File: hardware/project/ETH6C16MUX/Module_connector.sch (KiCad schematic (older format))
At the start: 5 parts, among them J901 Conn_02x12_Odd_Even

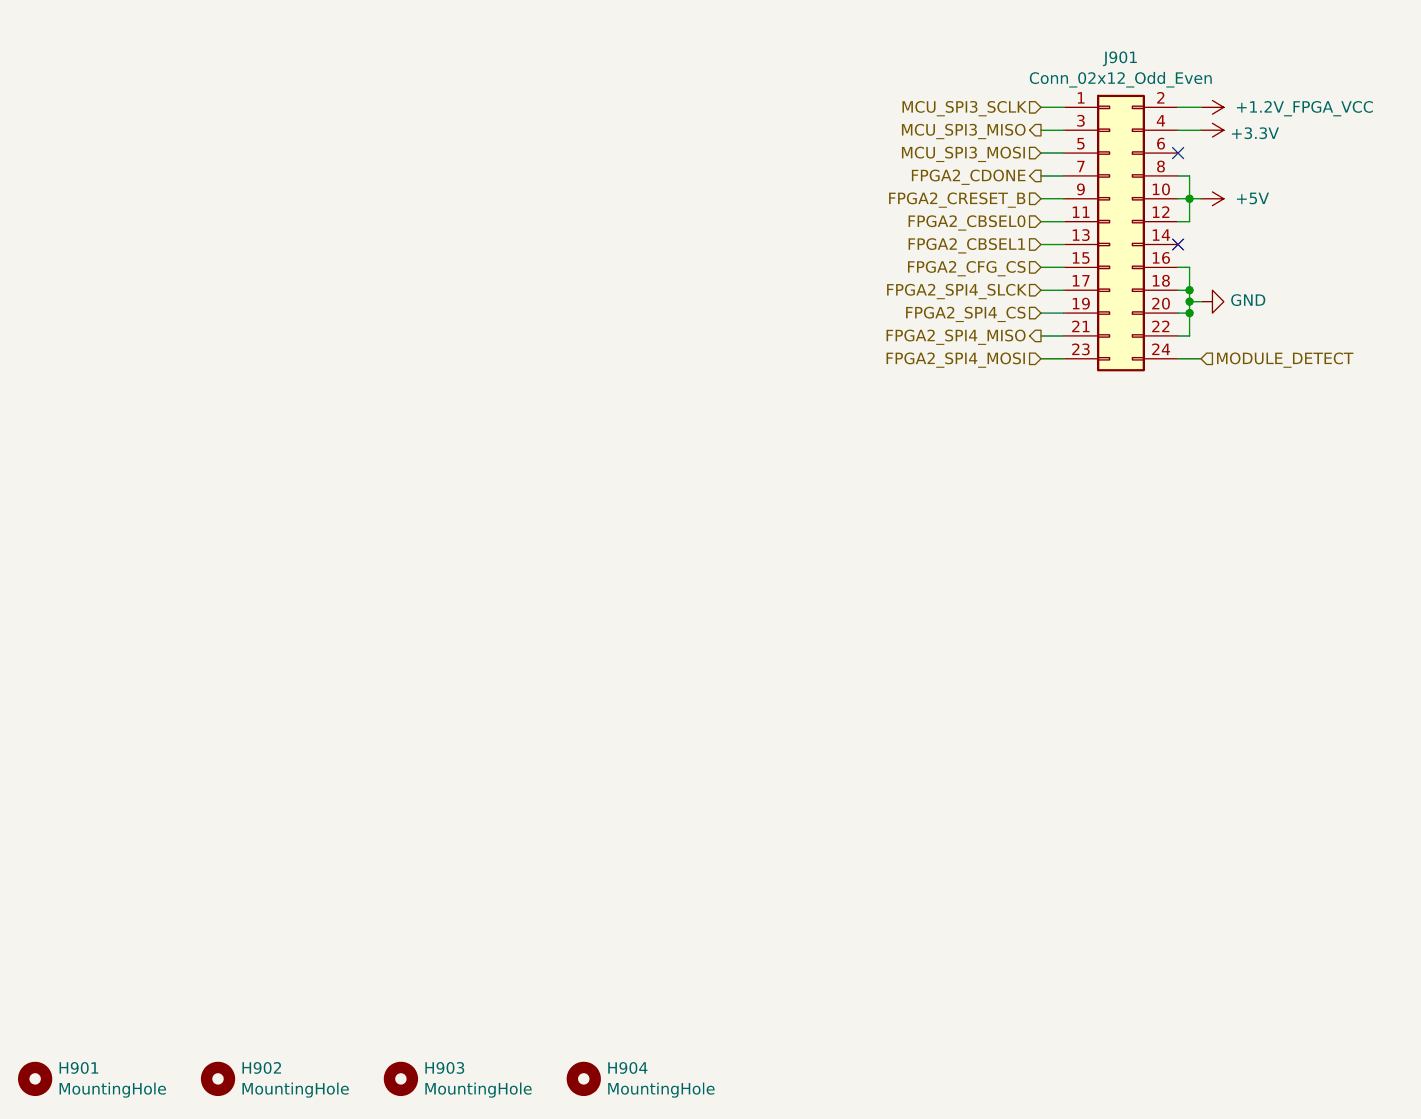
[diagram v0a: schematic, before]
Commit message: PCB design, need to redesign of the board to board connectors.
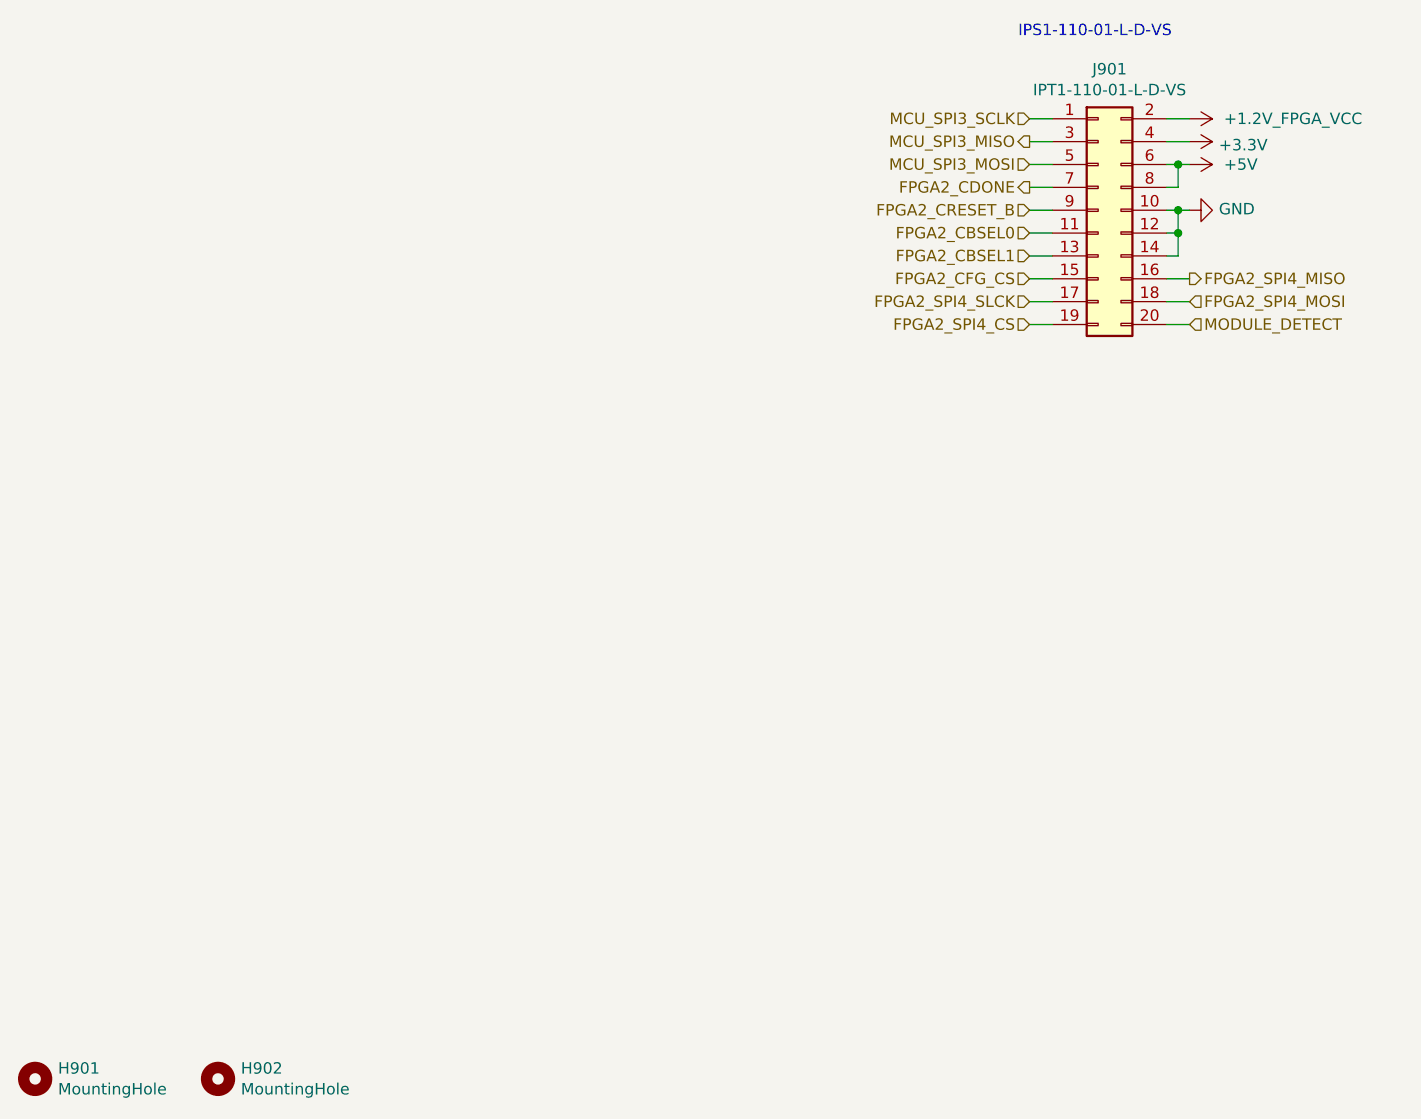
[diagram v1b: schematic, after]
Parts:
- removed H903, H904: MountingHole, symbol Mechanical:MountingHole
- removed J901: Conn_02x12_Odd_Even, symbol Connector_Generic:Conn_02x12_Odd_Even
- added J901: IPT1-110-01-L-D-VS, Connector_PinHeader_2.54mm:PinHeader_2x10_P2.54mm_Vertical_SMD, symbol Connector_Generic:Conn_02x10_Odd_Even
- H901, H902: footprint (none) -> MountingHole:MountingHole_3mm_Pad
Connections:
- net +1.2V_FPGA_VCC: now also J901.2 (Pin_2)
- net +3V3: now also J901.4 (Pin_4)
- net +5V: now also J901.6 (Pin_6), J901.8 (Pin_8)
- net FPGA2_CBSEL0: now also J901.11 (Pin_11)
- net FPGA2_CBSEL1: now also J901.13 (Pin_13)
- net FPGA2_CDONE: now also J901.7 (Pin_7)
- net FPGA2_CFG_CS: now also J901.15 (Pin_15)
- net FPGA2_CRESET_B: now also J901.9 (Pin_9)
- net FPGA2_SPI4_CS: now also J901.19 (Pin_19)
- net FPGA2_SPI4_MISO: now also J901.16 (Pin_16)
- net FPGA2_SPI4_MOSI: now also J901.18 (Pin_18)
- net FPGA2_SPI4_SLCK: now also J901.17 (Pin_17)
- net GND: now also J901.10 (Pin_10), J901.12 (Pin_12), J901.14 (Pin_14)
- net MCU_SPI3_MISO: now also J901.3 (Pin_3)
- net MCU_SPI3_MOSI: now also J901.5 (Pin_5)
- net MCU_SPI3_SCLK: now also J901.1 (Pin_1)
- net MODULE_DETECT: now also J901.20 (Pin_20)
- no-connect marks 2 -> 0
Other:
- note added: "IPS1-110-01-L-D-VS"
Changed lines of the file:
@@
 $EndDescr
-$Comp
-L Connector_Generic:Conn_02x12_Odd_Even J901
-U 1 1 5D9271DE
-P 5750 3250
-F 0 "J901" H 5800 3967 50  0000 C CNN
-F 1 "Conn_02x12_Odd_Even" H 5800 3876 50  0000 C CNN
-F 2 "" H 5750 3250 50  0001 C CNN
-F 3 "~" H 5750 3250 50  0001 C CNN
-	1    5750 3250
-	1    0    0    -1
-$EndComp
 $Comp
 L ETH6C16MUX:+1.2V_FPGA_VCC #PWR0901
 U 1 1 5D928C56
-P 6150 2750
-F 0 "#PWR0901" H 6150 2600 50  0001 C CNN
-F 1 "+1.2V_FPGA_VCC" V 6150 2900 50  0000 L CNN
-F 2 "" H 6150 2750 50  0001 C CNN
-F 3 "" H 6150 2750 50  0001 C CNN
-	1    6150 2750
+P 6100 2800
+F 0 "#PWR0901" H 6100 2650 50  0001 C CNN
+F 1 "+1.2V_FPGA_VCC" V 6100 2950 50  0000 L CNN
+F 2 "" H 6100 2800 50  0001 C CNN
+F 3 "" H 6100 2800 50  0001 C CNN
+	1    6100 2800
 	0    1    1    0
 $EndComp
-Text HLabel 5450 3450 0    50   Input ~ 0
+Text HLabel 5400 3500 0    50   Input ~ 0
 FPGA2_CFG_CS
-Text HLabel 5450 3850 0    50   Input ~ 0
+Text HLabel 6100 3600 2    50   Input ~ 0
 FPGA2_SPI4_MOSI
-Text HLabel 5450 3750 0    50   Output ~ 0
+Text HLabel 6100 3500 2    50   Output ~ 0
 FPGA2_SPI4_MISO
-Text HLabel 5450 3650 0    50   Input ~ 0
+Text HLabel 5400 3700 0    50   Input ~ 0
 FPGA2_SPI4_CS
-Text HLabel 5450 3550 0    50   Input ~ 0
+Text HLabel 5400 3600 0    50   Input ~ 0
 FPGA2_SPI4_SLCK
-Text HLabel 5450 3050 0    50   Output ~ 0
+Text HLabel 5400 3100 0    50   Output ~ 0
 FPGA2_CDONE
-Text HLabel 5450 3150 0    50   Input ~ 0
+Text HLabel 5400 3200 0    50   Input ~ 0
 FPGA2_CRESET_B
-Text HLabel 5450 3350 0    50   Input ~ 0
+Text HLabel 5400 3400 0    50   Input ~ 0
 FPGA2_CBSEL1
-Text HLabel 5450 3250 0    50   Input ~ 0
+Text HLabel 5400 3300 0    50   Input ~ 0
 FPGA2_CBSEL0
-Text HLabel 5450 2950 0    50   Input ~ 0
+Text HLabel 5400 3000 0    50   Input ~ 0
 MCU_SPI3_MOSI
-Text HLabel 5450 2850 0    50   Output ~ 0
+Text HLabel 5400 2900 0    50   Output ~ 0
 MCU_SPI3_MISO
-Text HLabel 5450 2750 0    50   Input ~ 0
+Text HLabel 5400 2800 0    50   Input ~ 0
 MCU_SPI3_SCLK
 $Comp
 L power:+5V #PWR0903
 U 1 1 5D938E43
-P 6150 3150
-F 0 "#PWR0903" H 6150 3000 50  0001 C CNN
-F 1 "+5V" V 6150 3300 50  0000 L CNN
-F 2 "" H 6150 3150 50  0001 C CNN
-F 3 "" H 6150 3150 50  0001 C CNN
-	1    6150 3150
+P 6100 3000
+F 0 "#PWR0903" H 6100 2850 50  0001 C CNN
+F 1 "+5V" V 6100 3150 50  0000 L CNN
+F 2 "" H 6100 3000 50  0001 C CNN
+F 3 "" H 6100 3000 50  0001 C CNN
+	1    6100 3000
 	0    1    1    0
 $EndComp
@@
 L power:GND #PWR0904
 U 1 1 5D93B202
-P 6150 3600
-F 0 "#PWR0904" H 6150 3350 50  0001 C CNN
-F 1 "GND" V 6155 3472 50  0000 R CNN
-F 2 "" H 6150 3600 50  0001 C CNN
-F 3 "" H 6150 3600 50  0001 C CNN
-	1    6150 3600
+P 6100 3200
+F 0 "#PWR0904" H 6100 2950 50  0001 C CNN
+F 1 "GND" V 6105 3072 50  0000 R CNN
+F 2 "" H 6100 3200 50  0001 C CNN
+F 3 "" H 6100 3200 50  0001 C CNN
+	1    6100 3200
 	0    -1   -1   0
 $EndComp
-Text HLabel 6150 3850 2    50   Input ~ 0
+Text HLabel 6100 3700 2    50   Input ~ 0
 MODULE_DETECT
 Wire Wire Line
-	5550 2750 5450 2750
+	5500 2800 5400 2800
 Wire Wire Line
-	5450 2850 5550 2850
+	5400 2900 5500 2900
 Wire Wire Line
-	5550 2950 5450 2950
+	5500 3000 5400 3000
 Wire Wire Line
-	5450 3050 5550 3050
+	5400 3100 5500 3100
 Wire Wire Line
-	5450 3150 5550 3150
+	5400 3200 5500 3200
 Wire Wire Line
-	5450 3250 5550 3250
+	5400 3300 5500 3300
 Wire Wire Line
-	5550 3350 5450 3350
+	5500 3400 5400 3400
 Wire Wire Line
-	5450 3450 5550 3450
+	5400 3500 5500 3500
 Wire Wire Line
-	5550 3550 5450 3550
+	5500 3600 5400 3600
 Wire Wire Line
-	5450 3650 5550 3650
+	5400 3700 5500 3700
 Wire Wire Line
-	5550 3750 5450 3750
+	6000 3500 6100 3500
 Wire Wire Line
-	5450 3850 5550 3850
+	6100 3600 6000 3600
 Wire Wire Line
-	6050 3450 6100 3450
-Wire Wire Line
-	6100 3450 6100 3550
-Wire Wire Line
-	6100 3650 6050 3650
-Wire Wire Line
-	6050 3550 6100 3550
-Connection ~ 6100 3550
-Wire Wire Line
-	6100 3550 6100 3600
-Wire Wire Line
-	6150 3600 6100 3600
-Wire Wire Line
-	6050 3050 6100 3050
-Wire Wire Line
-	6100 3050 6100 3150
-Wire Wire Line
-	6100 3250 6050 3250
-Wire Wire Line
-	6050 3150 6100 3150
-Connection ~ 6100 3150
-Wire Wire Line
-	6100 3150 6100 3250
-Wire Wire Line
-	6100 3150 6150 3150
-NoConn ~ 6050 3350
-NoConn ~ 6050 2950
-Wire Wire Line
-	6150 3850 6050 3850
-Wire Wire Line
-	6150 2850 6050 2850
-Wire Wire Line
-	6050 2750 6150 2750
+	6100 3700 6000 3700
 $Comp
 L Mechanical:MountingHole H901
@@
 F 0 "H901" H 1150 7046 50  0000 L CNN
 F 1 "MountingHole" H 1150 6955 50  0000 L CNN
-F 2 "" H 1050 7000 50  0001 C CNN
+F 2 "MountingHole:MountingHole_3mm_Pad" H 1050 7000 50  0001 C CNN
 F 3 "~" H 1050 7000 50  0001 C CNN
 	1    1050 7000
@@
 F 0 "H902" H 1950 7046 50  0000 L CNN
 F 1 "MountingHole" H 1950 6955 50  0000 L CNN
-F 2 "" H 1850 7000 50  0001 C CNN
+F 2 "MountingHole:MountingHole_3mm_Pad" H 1850 7000 50  0001 C CNN
 F 3 "~" H 1850 7000 50  0001 C CNN
 	1    1850 7000
@@
 $EndComp
 $Comp
-L Mechanical:MountingHole H903
-U 1 1 5D96F3DC
-P 2650 7000
-F 0 "H903" H 2750 7046 50  0000 L CNN
-F 1 "MountingHole" H 2750 6955 50  0000 L CNN
-F 2 "" H 2650 7000 50  0001 C CNN
-F 3 "~" H 2650 7000 50  0001 C CNN
-	1    2650 7000
-	1    0    0    -1
+L power:+3.3V #PWR0133
+U 1 1 5DAC34FD
+P 6100 2900
+F 0 "#PWR0133" H 6100 2750 50  0001 C CNN
+F 1 "+3.3V" V 6115 3028 50  0000 L CNN
+F 2 "" H 6100 2900 50  0001 C CNN
+F 3 "" H 6100 2900 50  0001 C CNN
+	1    6100 2900
+	0    1    1    0
 $EndComp
+Text Notes 5350 2450 0    50   ~ 0
+IPS1-110-01-L-D-VS
 $Comp
-L Mechanical:MountingHole H904
-U 1 1 5D96F5CE
-P 3450 7000
-F 0 "H904" H 3550 7046 50  0000 L CNN
-F 1 "MountingHole" H 3550 6955 50  0000 L CNN
-F 2 "" H 3450 7000 50  0001 C CNN
-F 3 "~" H 3450 7000 50  0001 C CNN
-	1    3450 7000
+L Connector_Generic:Conn_02x10_Odd_Even J901
+U 1 1 61C79D6A
+P 5700 3200
+F 0 "J901" H 5750 3817 50  0000 C CNN
+F 1 "IPT1-110-01-L-D-VS" H 5750 3726 50  0000 C CNN
+F 2 "Connector_PinHeader_2.54mm:PinHeader_2x10_P2.54mm_Vertical_SMD" H 5700 3200 50  0001 C CNN
+F 3 "~" H 5700 3200 50  0001 C CNN
+	1    5700 3200
 	1    0    0    -1
 $EndComp
 Wire Wire Line
-	6100 3650 6100 3750
+	6100 2800 6000 2800
 Wire Wire Line
-	6100 3750 6050 3750
-Connection ~ 6100 3650
-Connection ~ 6100 3600
+	6100 2900 6000 2900
 Wire Wire Line
-	6100 3600 6100 3650
-$Comp
-L power:+3.3V #PWR0133
-U 1 1 5DAC34FD
-P 6150 2850
-F 0 "#PWR0133" H 6150 2700 50  0001 C CNN
-F 1 "+3.3V" V 6165 2978 50  0000 L CNN
-F 2 "" H 6150 2850 50  0001 C CNN
-F 3 "" H 6150 2850 50  0001 C CNN
-	1    6150 2850
-	0    1    1    0
-$EndComp
+	6000 3100 6050 3100
+Wire Wire Line
+	6050 3100 6050 3000
+Wire Wire Line
+	6050 3000 6000 3000
+Wire Wire Line
+	6050 3000 6100 3000
+Connection ~ 6050 3000
+Wire Wire Line
+	6000 3200 6050 3200
+Wire Wire Line
+	6050 3200 6050 3300
+Wire Wire Line
+	6050 3400 6000 3400
+Wire Wire Line
+	6000 3300 6050 3300
+Connection ~ 6050 3300
+Wire Wire Line
+	6050 3300 6050 3400
+Connection ~ 6050 3200
+Wire Wire Line
+	6100 3200 6050 3200
 $EndSCHEMATC
